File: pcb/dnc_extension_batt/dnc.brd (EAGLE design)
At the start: 99.8 x 56 mm, 105 parts, among them Q1 IRF9321PBF, Q2 IRF9321PBF, Q3 BSS138, Q5 BSS138, U1 LCD-16X2NOHOLES, U2 74HCT595D

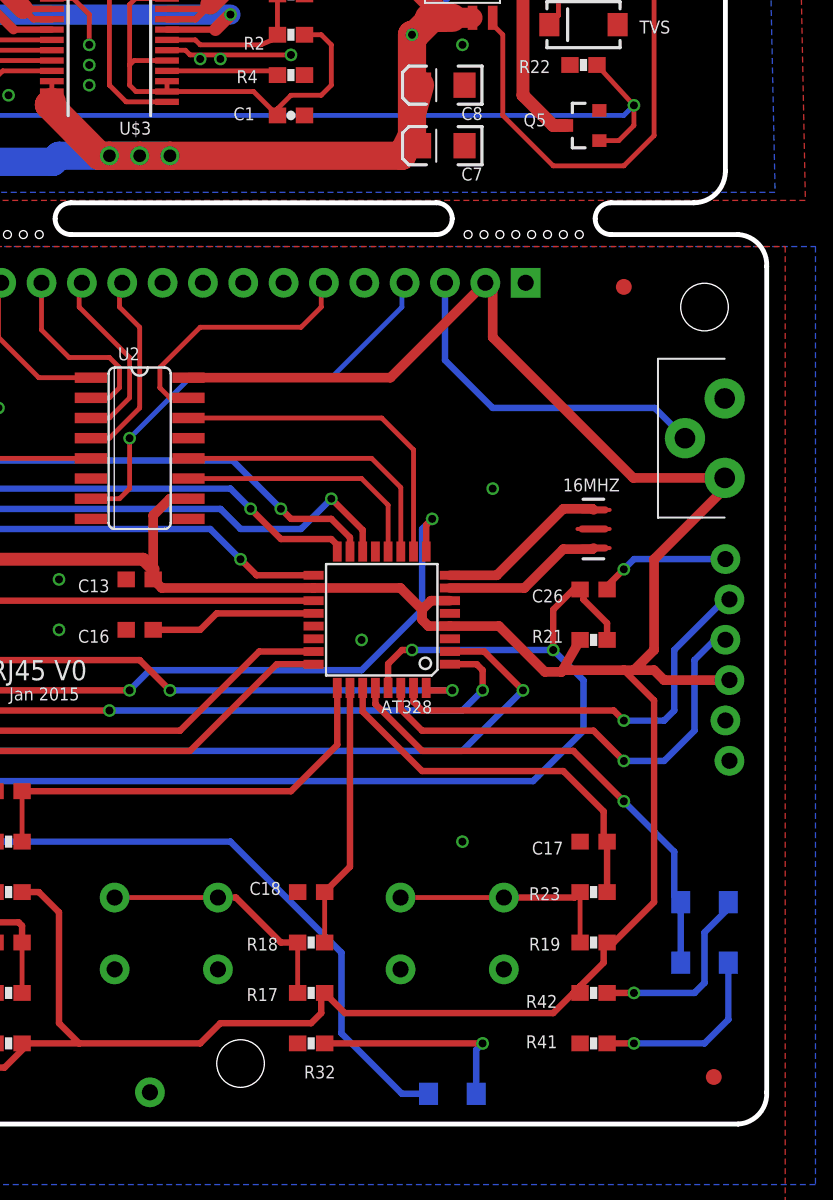
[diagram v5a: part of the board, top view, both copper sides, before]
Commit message: change minor : - add rj45 for led string - add select pam led or flex
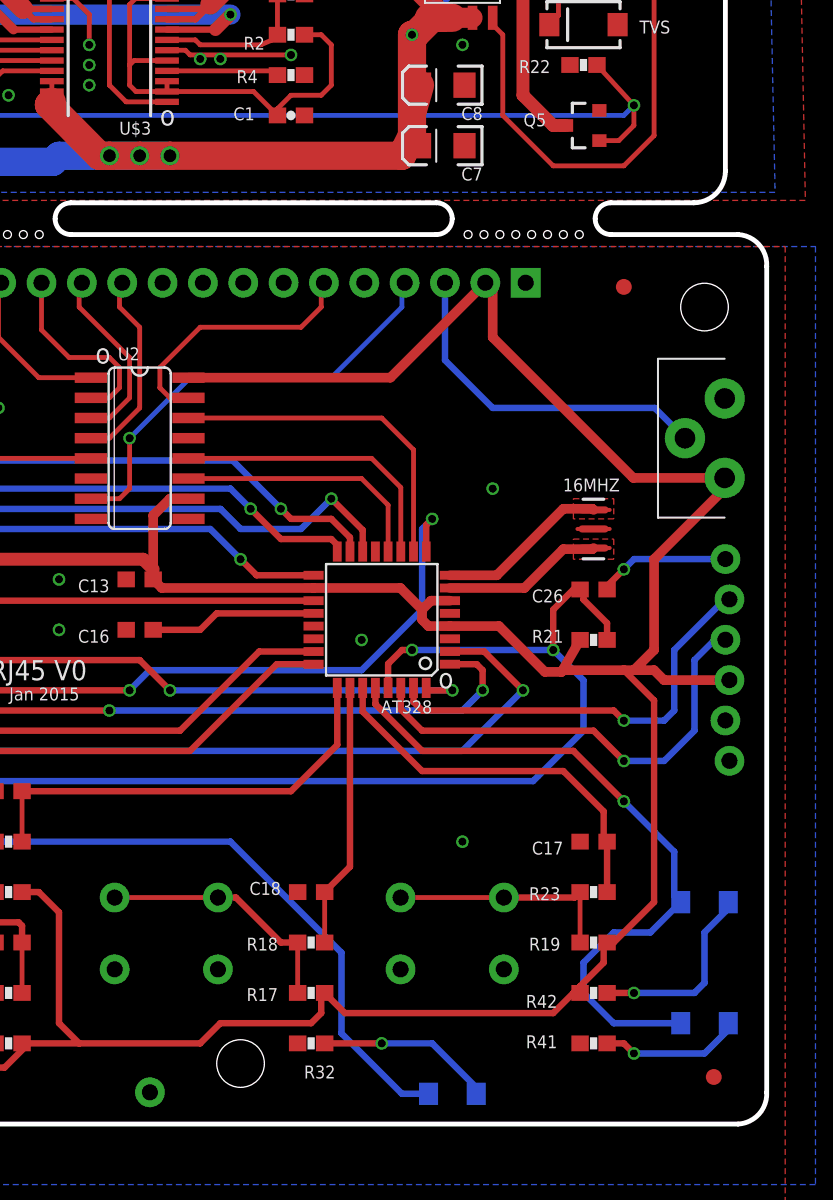
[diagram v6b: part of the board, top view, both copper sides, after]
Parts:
- removed L5: LG, SparkFun-LED:LED-1206
- added L2: LG, SparkFun-LED:LED-1206
- turned L3 to 180 degrees
- renumbered L6 to L3
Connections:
- net LED-PUSH3: now also L3.A; no longer L3.C
- net N$30: now also L2.C; no longer L5.A
- net N$35: now also L3.C; no longer L3.A
- net WARNING: now also L2.A; no longer L5.C
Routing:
- net WARNING: track 30.8 -> 43.5 mm
- net N$30: track 11.8 -> 8.92 mm
- net N$35: track 13.3 -> 11.1 mm
- added copper zone on layer 1, net N$37
- added copper zone on layer 1, net N$39
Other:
- board text added: "o"
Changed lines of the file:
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@@
 <text x="74.295" y="93.98" size="0.8128" layer="48" ratio="10">RPI+ 10mm</text>
 <text x="27.305" y="93.98" size="0.8128" layer="48" ratio="10">RPI+ 10mm</text>
+<text x="79.121" y="27.432" size="1.27" layer="21" font="vector" ratio="20">o</text>
+<text x="57.531" y="47.879" size="1.27" layer="21" font="vector" ratio="20">o</text>
+<text x="61.595" y="62.865" size="1.27" layer="21" font="vector" ratio="20">o</text>
 </plain>
 <attributes>
@@
 <attribute name="VALUE" x="94.361" y="8.763" size="0.8128" layer="27" font="vector" rot="R180"/>
 </element>
-<element name="L5" library="SparkFun-LED" package="LED-1206" value="LG" x="95.885" y="10.16" smashed="yes" rot="MR0">
-<attribute name="NAME" x="92.329" y="9.652" size="0.8128" layer="26" rot="MR0"/>
-<attribute name="VALUE" x="96.901" y="8.382" size="0.4064" layer="28" rot="MR0"/>
-</element>
 <element name="R41" library="SparkFun-Passives" package="0603-RES" value="1K" x="88.9" y="5.08" smashed="yes" rot="R180">
 <attribute name="NAME" x="86.614" y="5.588" size="0.8128" layer="25" font="vector" rot="R180"/>
@@
 <attribute name="VALUE" x="48.895" y="46.99" size="0.8128" layer="27" rot="R180"/>
 <attribute name="P" value="250mw" x="46.355" y="46.355" size="1.778" layer="27" rot="R180" display="off"/>
-</element>
-<element name="L6" library="SparkFun-LED" package="LED-1206" value="LG" x="80.01" y="1.905" smashed="yes" rot="MR0">
-<attribute name="NAME" x="85.344" y="1.397" size="0.8128" layer="26" rot="MR0"/>
-<attribute name="VALUE" x="81.026" y="0.127" size="0.4064" layer="28" rot="MR0"/>
 </element>
 <element name="R32" library="SparkFun-Passives" package="0603-RES" value="1K" x="71.12" y="5.08" smashed="yes" rot="R180">
@@
 <element name="JP3" library="SparkFun" package="FIDUCIAL-1X2.5" value="FIDUCIAL1X2.5" x="10.16" y="13.97"/>
 <element name="JP4" library="SparkFun" package="FIDUCIAL-1X2.5" value="FIDUCIAL1X2.5" x="90.805" y="52.705"/>
+<element name="L2" library="SparkFun-LED" package="LED-1206" value="LG" x="95.885" y="6.35" rot="MR180"/>
+<element name="L3" library="SparkFun-LED" package="LED-1206" value="LG" x="80.01" y="1.905" rot="MR180"/>
 </elements>
 <signals>
@@
 <wire x1="89.75" y1="8.255" x2="91.44" y2="8.255" width="0.4064" layer="1"/>
 </signal>
-<signal name="N$30">
-<contactref element="L5" pad="A"/>
-<contactref element="R41" pad="1"/>
-<wire x1="97.385" y1="10.16" x2="97.385" y2="6.58" width="0.4064" layer="16"/>
-<wire x1="97.385" y1="6.58" x2="95.885" y2="5.08" width="0.4064" layer="16"/>
-<wire x1="95.885" y1="5.08" x2="91.44" y2="5.08" width="0.4064" layer="16"/>
-<via x="91.44" y="5.08" extent="1-16" drill="0.5"/>
-<wire x1="89.75" y1="5.08" x2="91.44" y2="5.08" width="0.4064" layer="1"/>
-</signal>
 <signal name="N$23">
 <contactref element="U$7" pad="A"/>
@@
 </signal>
 <signal name="WARNING">
-<contactref element="L5" pad="C"/>
 <contactref element="L4" pad="C"/>
-<wire x1="94.385" y1="10.16" x2="94.385" y2="13.97" width="0.4064" layer="16"/>
 <contactref element="AT328" pad="28"/>
 <wire x1="75.165" y1="27.4574" x2="75.165" y2="26.435" width="0.4064" layer="1"/>
@@
 <wire x1="93.98" y1="17.145" x2="93.98" y2="14.375" width="0.4064" layer="16"/>
 <wire x1="93.98" y1="14.375" x2="94.385" y2="13.97" width="0.4064" layer="16"/>
+<contactref element="L2" pad="A"/>
+<wire x1="94.385" y1="6.35" x2="90.17" y2="6.35" width="0.4064" layer="16"/>
+<wire x1="90.17" y1="6.35" x2="88.265" y2="8.255" width="0.4064" layer="16"/>
+<wire x1="88.265" y1="8.255" x2="88.265" y2="10.16" width="0.4064" layer="16"/>
+<wire x1="88.265" y1="10.16" x2="90.17" y2="12.065" width="0.4064" layer="16"/>
+<wire x1="90.17" y1="12.065" x2="92.48" y2="12.065" width="0.4064" layer="16"/>
+<wire x1="92.48" y1="12.065" x2="94.385" y2="13.97" width="0.4064" layer="16"/>
 </signal>
 <signal name="N$38">
@@
 </signal>
 <signal name="LED-PUSH3">
-<contactref element="L6" pad="C"/>
 <contactref element="AT328" pad="23"/>
 <wire x1="71.2724" y1="29.75" x2="67.85" y2="29.75" width="0.4064" layer="1"/>
@@
 <wire x1="73.025" y1="10.795" x2="73.025" y2="5.715" width="0.4064" layer="16"/>
 <wire x1="73.025" y1="5.715" x2="76.835" y2="1.905" width="0.4064" layer="16"/>
-<wire x1="76.835" y1="1.905" x2="78.51" y2="1.905" width="0.4064" layer="16"/>
-</signal>
-<signal name="N$35">
-<contactref element="L6" pad="A"/>
-<contactref element="R32" pad="1"/>
-<via x="81.915" y="5.08" extent="1-16" drill="0.5"/>
-<wire x1="71.97" y1="5.08" x2="81.915" y2="5.08" width="0.4064" layer="1"/>
-<wire x1="81.51" y1="1.905" x2="81.51" y2="4.675" width="0.4064" layer="16"/>
-<wire x1="81.51" y1="4.675" x2="81.915" y2="5.08" width="0.4064" layer="16"/>
+<contactref element="L3" pad="A"/>
+<wire x1="78.51" y1="1.905" x2="76.835" y2="1.905" width="0.4064" layer="16"/>
 </signal>
 <signal name="N$33">
@@
 <wire x1="20.955" y1="45.505" x2="20.74" y2="45.72" width="0.4064" layer="1"/>
 </signal>
+<signal name="N$30">
+<contactref element="R41" pad="1"/>
+<contactref element="L2" pad="C"/>
+<wire x1="97.385" y1="6.35" x2="97.385" y2="5.945" width="0.4064" layer="16"/>
+<wire x1="97.385" y1="5.945" x2="95.885" y2="4.445" width="0.4064" layer="16"/>
+<wire x1="95.885" y1="4.445" x2="91.44" y2="4.445" width="0.4064" layer="16"/>
+<via x="91.44" y="4.445" extent="1-16" drill="0.5"/>
+<wire x1="89.75" y1="5.08" x2="90.805" y2="5.08" width="0.4064" layer="1"/>
+<wire x1="90.805" y1="5.08" x2="91.44" y2="4.445" width="0.4064" layer="1"/>
+</signal>
+<signal name="N$35">
+<contactref element="R32" pad="1"/>
+<contactref element="L3" pad="C"/>
+<wire x1="81.51" y1="1.905" x2="81.51" y2="2.31" width="0.4064" layer="16"/>
+<wire x1="81.51" y1="2.31" x2="78.74" y2="5.08" width="0.4064" layer="16"/>
+<wire x1="78.74" y1="5.08" x2="75.565" y2="5.08" width="0.4064" layer="16"/>
+<via x="75.565" y="5.08" extent="1-16" drill="0.5"/>
+<wire x1="71.97" y1="5.08" x2="75.565" y2="5.08" width="0.4064" layer="1"/>
+</signal>
+<signal name="N$37">
+<polygon width="0" layer="1" pour="cutout">
+<vertex x="87.63" y="36.83"/>
+<vertex x="90.17" y="36.83"/>
+<vertex x="90.17" y="35.56"/>
+<vertex x="87.63" y="35.56"/>
+</polygon>
+</signal>
+<signal name="N$39">
+<polygon width="0" layer="1" pour="cutout">
+<vertex x="87.63" y="38.1"/>
+<vertex x="87.63" y="39.37"/>
+<vertex x="90.17" y="39.37"/>
+<vertex x="90.17" y="38.1"/>
+</polygon>
+</signal>
 </signals>

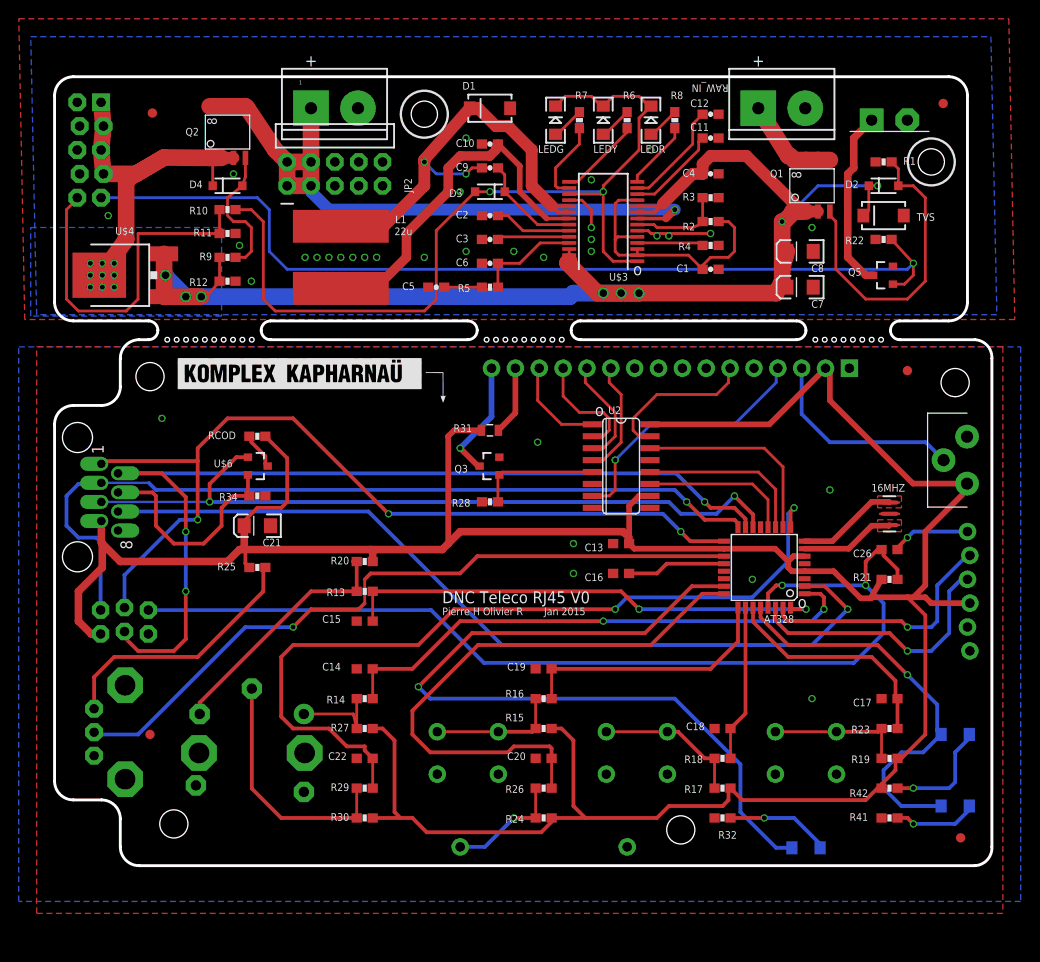
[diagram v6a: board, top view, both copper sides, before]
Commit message: major changes : - carte pieuvre - carte relais - correctif v1 : usb + pin A7 ! - enclosure
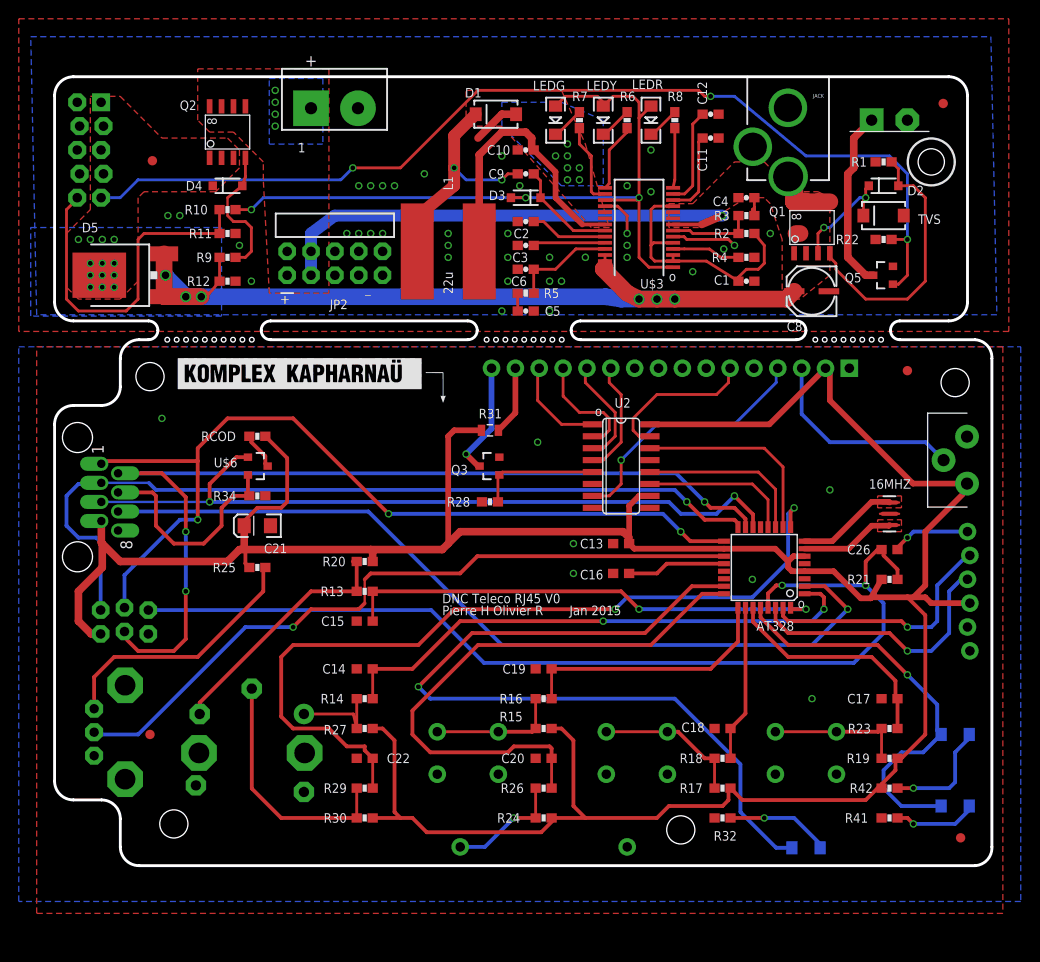
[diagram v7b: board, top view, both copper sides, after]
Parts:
- removed C7: 22u, SparkFun-Passives:EIA3216
- removed RAW_IN: SUPPLY, pierre_vv:DNC_IN2_PWR
- added JACK: POWER_JACKPTH_LOCK, SparkFun:POWER_JACK_PTH_LOCK
- C8: device SparkFun-Passives:EIA3216 -> SparkFun-Passives:PANASONIC_C
- moved L1 11.4 mm to (41.9, 65.4), turned to 180 degrees
- moved C5 9.86 mm to (50.2, 59.1), turned to 0 degrees
- moved JP2 9.52 mm to (29.8, 64.1)
- moved JP13 5.08 mm to (10.4, 75.1)
- moved C8 4.62 mm to (80.6, 61.0)
- moved C4 4.58 mm to (73.7, 71.1)
- moved Q1 4.45 mm to (80.6, 67.9)
- moved R3 4.26 mm to (73.7, 69.2)
- moved R4 4.02 mm to (73.7, 64.8)
- moved C1 4.02 mm to (73.7, 62.2)
- moved R2 4.02 mm to (73.7, 67.3)
- moved C2 3.86 mm to (50.2, 68.6)
- moved C6 3.86 mm to (50.2, 63.5)
- moved C9 3.86 mm to (50.2, 73.7)
- moved R5 3.86 mm to (50.2, 61.0)
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- renumbered U$4 to D5
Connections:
- net GND: now also C8.-, JACK.GND, JACK.GNDBREAK; no longer C7.C, C8.C, RAW_IN.2
- net N$13: now also LEDY.C; no longer LEDY.A
- net N$14: now also LEDG.C; no longer LEDG.A
- net N$15: now also LEDR.C; no longer LEDR.A
- net RAW_POL_PROTECTED: now also C8.+; no longer C7.A, C8.A
- net RAW_UNPROTECTED1: now also JACK.PWR; no longer RAW_IN.1
- net VL: now also LEDG.A, LEDR.A, LEDY.A; no longer LEDG.C, LEDR.C, LEDY.C
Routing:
- net RAW_POL_PROTECTED: track 146.9 -> 105.1 mm
- net SYSTEM_LOAD: track 41.2 -> 0.32 mm, vias 9 -> 13
- net N$3: track 46.9 -> 25.0 mm, vias 2 -> 9
- net V+BATT: track 71.7 -> 54.4 mm, vias 1 -> 5
- net VL: track 95.2 -> 81.8 mm, vias 2 -> 3
- net RELAY_CHARGE_BOARD: track 99.9 -> 108.4 mm, vias 1 -> 3
- net GND: track 12.6 -> 20.9 mm, vias 33 -> 44
- net N$18: track 38.8 -> 31.0 mm
- net PROTECT_GATE: track 33.2 -> 28.7 mm
- net RAW_UNPROTECTED1: track 10.6 -> 6.64 mm
- net N$6: track 4.02 -> 1.91 mm
- net N$1: track 29.7 -> 28.1 mm
- net N$10: track 8.78 -> 7.33 mm
- net N$12: track 7.37 -> 6.38 mm
- net N$16: track 9.92 -> 8.98 mm
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- added copper zone on layer 1, net N$3
- added copper zone on layer 16, net N$3
- added copper zone on layer 1, net RAW_POL_PROTECTED
- added copper zone on layer 1, net SYSTEM_LOAD
- added copper zone on layer 1, net V+BATT
- added copper zone on layer 16, net V+BATT
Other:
- board text added: "_"
